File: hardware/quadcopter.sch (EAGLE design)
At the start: 56 parts, among them J1 AVR_SPI_PRG_6NS, J2 HEADER-4POS-2X2-0.1IN-FEMALE-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, J3 HEADER-10POSTH-254X10, J4 HEADER-4POS-0.1IN-FEMALE-SMD-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, Q1 MOSFET-SI2302CDS-T1-E3CT-ND, Q5 MOSFET-SI2302CDS-T1-E3CT-ND, Q6 MOSFET-SI2302CDS-T1-E3CT-ND, SW1 PUSHBUTTON_SMD-VERTICAL-1, U1 ATMEGA128RFA1, U2 LSM-IMU-497-18367-1-NDIMU, Y1 CRYSTAL5X3

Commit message: replaced motors
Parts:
- added MOTOR2, MOTOR3, MOTOR4: MOTOR_PADS_GND-MOLEX-SMD, quadparts_prebuilt_2022:MOTOR_PADS_GND-MOLEX-SMD
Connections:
- net BAT_GND: now also MOTOR2.GND, MOTOR3.GND, MOTOR4.GND
- net N$15: now also MOTOR2.V-
- net N$16: now also MOTOR3.V-
- net N$17: now also MOTOR4.V-
- net VBAT: now also MOTOR2.V+, MOTOR3.V+, MOTOR4.V+
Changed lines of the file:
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@@
 <part name="GND47" library="quadparts_prebuilt_2022" deviceset="GND" device=""/>
 <part name="P+22" library="quadparts_prebuilt_2022" deviceset="3V" device=""/>
+<part name="MOTOR2" library="quadparts_prebuilt_2022" deviceset="MOTOR_PADS_GND" device="-MOLEX-SMD"/>
+<part name="MOTOR3" library="quadparts_prebuilt_2022" deviceset="MOTOR_PADS_GND" device="-MOLEX-SMD"/>
+<part name="MOTOR4" library="quadparts_prebuilt_2022" deviceset="MOTOR_PADS_GND" device="-MOLEX-SMD"/>
 </parts>
 <sheets>
@@
 <attribute name="VALUE" x="256.54" y="27.94" size="1.778" layer="96" rot="R180" align="center"/>
 </instance>
+<instance part="MOTOR2" gate="G$1" x="55.88" y="27.94" smashed="yes">
+<attribute name="NAME" x="53.34" y="35.56" size="0.8128" layer="95"/>
+</instance>
+<instance part="MOTOR3" gate="G$1" x="104.14" y="27.94" smashed="yes">
+<attribute name="NAME" x="101.6" y="35.56" size="0.8128" layer="95"/>
+</instance>
+<instance part="MOTOR4" gate="G$1" x="154.94" y="27.94" smashed="yes">
+<attribute name="NAME" x="152.4" y="35.56" size="0.8128" layer="95"/>
+</instance>
 </instances>
 <busses>
@@
 <junction x="63.5" y="38.1"/>
 <pinref part="D4" gate="G$1" pin="C"/>
+<pinref part="MOTOR2" gate="G$1" pin="V+"/>
 </segment>
 <segment>
@@
 <junction x="111.76" y="38.1"/>
 <pinref part="D5" gate="G$1" pin="C"/>
+<pinref part="MOTOR3" gate="G$1" pin="V+"/>
 </segment>
 <segment>
@@
 <junction x="162.56" y="38.1"/>
 <pinref part="D6" gate="G$1" pin="C"/>
+<pinref part="MOTOR4" gate="G$1" pin="V+"/>
 </segment>
 <segment>
@@
 <pinref part="C15" gate="G$1" pin="2"/>
 </segment>
+<segment>
+<pinref part="GND23" gate="1" pin="BAT_GND"/>
+<pinref part="MOTOR2" gate="G$1" pin="GND"/>
+</segment>
+<segment>
+<pinref part="GND26" gate="1" pin="BAT_GND"/>
+<pinref part="MOTOR3" gate="G$1" pin="GND"/>
+</segment>
+<segment>
+<pinref part="GND29" gate="1" pin="BAT_GND"/>
+<pinref part="MOTOR4" gate="G$1" pin="GND"/>
+</segment>
 </net>
 <net name="PWM2" class="0">
@@
 <wire x1="86.36" y1="27.94" x2="86.36" y2="25.4" width="0.1524" layer="91"/>
 <pinref part="D4" gate="G$1" pin="A"/>
+<pinref part="MOTOR2" gate="G$1" pin="V-"/>
 </segment>
 </net>
@@
 <pinref part="D5" gate="G$1" pin="A"/>
 <junction x="124.46" y="27.94"/>
+<pinref part="MOTOR3" gate="G$1" pin="V-"/>
 </segment>
 </net>
@@
 <wire x1="185.42" y1="27.94" x2="185.42" y2="25.4" width="0.1524" layer="91"/>
 <pinref part="D6" gate="G$1" pin="A"/>
-</segment>
-</net>
+<pinref part="MOTOR4" gate="G$1" pin="V-"/>
+</segment>
+</net>

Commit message: replaced motor pads and mosfets fulls
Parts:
- added Q2, Q3, Q4: MOSFET-SI2302CDS-T1-E3CT-ND, custom_.lbr:MOSFET-SI2302CDS-T1-E3CT-ND
- renumbered FRONT-LEFT-MOTOR to U$1
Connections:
- net BAT_GND: now also Q2.S, Q3.S, Q4.S
- net N$15: now also Q2.D
- net N$16: now also Q3.D
- net N$17: now also Q4.D
- net PWM2: now also Q2.G
- net PWM3: now also Q3.G
- net PWM4: now also Q4.G
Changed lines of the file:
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@@
 <part name="GND18" library="quadparts_prebuilt_2022" deviceset="GND" device=""/>
 <part name="P+7" library="quadparts_prebuilt_2022" deviceset="3V" device=""/>
-<part name="FRONT-LEFT-MOTOR" library="quadparts_prebuilt_2022" deviceset="MOTOR_PADS_GND" device="-MOLEX-SMD"/>
 <part name="P+8" library="quadparts_prebuilt_2022" deviceset="VBAT" device=""/>
 <part name="D3" library="quadparts_prebuilt_2022" deviceset="DIODE-SCHOTTKY_" device="-SMD-SOD123" package3d_urn="urn:adsk.eagle:package:11793366/1" value="360mV"/>
@@
 <part name="GND21" library="quadparts_prebuilt_2022" deviceset="BAT_GND" device=""/>
 <part name="GND22" library="quadparts_prebuilt_2022" deviceset="GND" device=""/>
-<part name="Q1" library="custom_.lbr" library_urn="urn:adsk.wipprod:fs.file:vf.FjMADskDQ2Se9fX1PD5xcw" deviceset="MOSFET" device="-SI2302CDS-T1-E3CT-ND"/>
 <part name="P+9" library="quadparts_prebuilt_2022" deviceset="VBAT" device=""/>
 <part name="D4" library="quadparts_prebuilt_2022" deviceset="DIODE-SCHOTTKY_" device="-SMD-SOD123" package3d_urn="urn:adsk.eagle:package:11793366/1" value="360mV"/>
@@
 <part name="MOTOR3" library="quadparts_prebuilt_2022" deviceset="MOTOR_PADS_GND" device="-MOLEX-SMD"/>
 <part name="MOTOR4" library="quadparts_prebuilt_2022" deviceset="MOTOR_PADS_GND" device="-MOLEX-SMD"/>
+<part name="U$1" library="quadparts_prebuilt_2022" deviceset="MOTOR_PADS_GND" device="-MOLEX-SMD"/>
+<part name="Q1" library="custom_.lbr" library_urn="urn:adsk.wipprod:fs.file:vf.FjMADskDQ2Se9fX1PD5xcw" deviceset="MOSFET" device="-SI2302CDS-T1-E3CT-ND"/>
+<part name="Q2" library="custom_.lbr" library_urn="urn:adsk.wipprod:fs.file:vf.FjMADskDQ2Se9fX1PD5xcw" deviceset="MOSFET" device="-SI2302CDS-T1-E3CT-ND"/>
+<part name="Q3" library="custom_.lbr" library_urn="urn:adsk.wipprod:fs.file:vf.FjMADskDQ2Se9fX1PD5xcw" deviceset="MOSFET" device="-SI2302CDS-T1-E3CT-ND"/>
+<part name="Q4" library="custom_.lbr" library_urn="urn:adsk.wipprod:fs.file:vf.FjMADskDQ2Se9fX1PD5xcw" deviceset="MOSFET" device="-SI2302CDS-T1-E3CT-ND"/>
 </parts>
 <sheets>
@@
 <attribute name="VALUE" x="287.02" y="162.56" size="1.778" layer="96" rot="R180" align="center"/>
 </instance>
-<instance part="FRONT-LEFT-MOTOR" gate="G$1" x="7.62" y="27.94" smashed="yes">
-<attribute name="NAME" x="5.08" y="35.56" size="0.8128" layer="95"/>
-</instance>
 <instance part="P+8" gate="VCC" x="-2.54" y="43.18" smashed="yes">
 <attribute name="VALUE" x="-2.54" y="45.72" size="1.778" layer="96" rot="R180" align="center"/>
@@
 <attribute name="VALUE" x="10.16" y="-5.08" size="1.778" layer="96" align="center"/>
 </instance>
-<instance part="Q1" gate="G$1" x="35.56" y="15.24" smashed="yes">
-<attribute name="NAME" x="27.94" y="20.32" size="1.778" layer="95"/>
-</instance>
 <instance part="P+9" gate="VCC" x="45.72" y="43.18" smashed="yes">
 <attribute name="VALUE" x="45.72" y="45.72" size="1.778" layer="96" rot="R180" align="center"/>
@@
 <instance part="MOTOR4" gate="G$1" x="154.94" y="27.94" smashed="yes">
 <attribute name="NAME" x="152.4" y="35.56" size="0.8128" layer="95"/>
+</instance>
+<instance part="U$1" gate="G$1" x="7.62" y="27.94" smashed="yes">
+<attribute name="NAME" x="5.08" y="35.56" size="0.8128" layer="95"/>
+</instance>
+<instance part="Q1" gate="G$1" x="35.56" y="15.24" smashed="yes">
+<attribute name="NAME" x="27.94" y="20.32" size="1.778" layer="95"/>
+</instance>
+<instance part="Q2" gate="G$1" x="83.82" y="15.24" smashed="yes">
+<attribute name="NAME" x="76.2" y="20.32" size="1.778" layer="95"/>
+</instance>
+<instance part="Q3" gate="G$1" x="132.08" y="15.24" smashed="yes">
+<attribute name="NAME" x="124.46" y="20.32" size="1.778" layer="95"/>
+</instance>
+<instance part="Q4" gate="G$1" x="182.88" y="15.24" smashed="yes">
+<attribute name="NAME" x="175.26" y="20.32" size="1.778" layer="95"/>
 </instance>
 </instances>
@@
 <net name="VBAT" class="0">
 <segment>
-<pinref part="FRONT-LEFT-MOTOR" gate="G$1" pin="V+"/>
 <wire x1="15.24" y1="33.02" x2="15.24" y2="38.1" width="0.1524" layer="91" style="longdash"/>
 <wire x1="15.24" y1="38.1" x2="-2.54" y2="38.1" width="0.1524" layer="91"/>
@@
 <pinref part="D3" gate="G$1" pin="C"/>
 <pinref part="C12" gate="G$1" pin="+"/>
+<pinref part="U$1" gate="G$1" pin="V+"/>
 </segment>
 <segment>
@@
 <wire x1="27.94" y1="30.48" x2="27.94" y2="27.94" width="0.1524" layer="91"/>
 <wire x1="27.94" y1="27.94" x2="15.24" y2="27.94" width="0.1524" layer="91"/>
-<pinref part="FRONT-LEFT-MOTOR" gate="G$1" pin="V-"/>
 <wire x1="27.94" y1="27.94" x2="38.1" y2="27.94" width="0.1524" layer="91"/>
 <junction x="27.94" y="27.94"/>
 <wire x1="38.1" y1="27.94" x2="38.1" y2="25.4" width="0.1524" layer="91"/>
+<pinref part="D3" gate="G$1" pin="A"/>
+<pinref part="U$1" gate="G$1" pin="V-"/>
 <pinref part="Q1" gate="G$1" pin="D"/>
-<pinref part="D3" gate="G$1" pin="A"/>
 </segment>
 </net>
 <net name="BAT_GND" class="0">
 <segment>
-<pinref part="FRONT-LEFT-MOTOR" gate="G$1" pin="GND"/>
 <pinref part="GND20" gate="1" pin="BAT_GND"/>
 <wire x1="-5.08" y1="25.4" x2="-5.08" y2="22.86" width="0.1524" layer="91"/>
 <wire x1="-5.08" y1="22.86" x2="7.62" y2="22.86" width="0.1524" layer="91"/>
+<pinref part="C12" gate="G$1" pin="-"/>
+<pinref part="U$1" gate="G$1" pin="GND"/>
 <junction x="7.62" y="22.86"/>
-<pinref part="C12" gate="G$1" pin="-"/>
-</segment>
-<segment>
-<pinref part="Q1" gate="G$1" pin="S"/>
+</segment>
+<segment>
 <wire x1="38.1" y1="5.08" x2="27.94" y2="5.08" width="0.1524" layer="91"/>
 <pinref part="GND21" gate="1" pin="BAT_GND"/>
+<pinref part="Q1" gate="G$1" pin="S"/>
 </segment>
 <segment>
 <wire x1="86.36" y1="5.08" x2="76.2" y2="5.08" width="0.1524" layer="91"/>
 <pinref part="GND24" gate="1" pin="BAT_GND"/>
+<pinref part="Q2" gate="G$1" pin="S"/>
 </segment>
 <segment>
 <wire x1="134.62" y1="5.08" x2="124.46" y2="5.08" width="0.1524" layer="91"/>
 <pinref part="GND27" gate="1" pin="BAT_GND"/>
+<pinref part="Q3" gate="G$1" pin="S"/>
 </segment>
 <segment>
 <wire x1="185.42" y1="5.08" x2="175.26" y2="5.08" width="0.1524" layer="91"/>
 <pinref part="GND30" gate="1" pin="BAT_GND"/>
+<pinref part="Q4" gate="G$1" pin="S"/>
 </segment>
 <segment>
@@
 <label x="66.04" y="22.86" size="1.016" layer="95" rot="R180" xref="yes"/>
 <pinref part="R7" gate="G$1" pin="1"/>
+<pinref part="Q2" gate="G$1" pin="G"/>
 </segment>
 <segment>
@@
 <pinref part="D4" gate="G$1" pin="A"/>
 <pinref part="MOTOR2" gate="G$1" pin="V-"/>
+<pinref part="Q2" gate="G$1" pin="D"/>
 </segment>
 </net>
@@
 <junction x="124.46" y="27.94"/>
 <pinref part="MOTOR3" gate="G$1" pin="V-"/>
+<pinref part="Q3" gate="G$1" pin="D"/>
 </segment>
 </net>
@@
 <pinref part="D6" gate="G$1" pin="A"/>
 <pinref part="MOTOR4" gate="G$1" pin="V-"/>
+<pinref part="Q4" gate="G$1" pin="D"/>
 </segment>
 </net>
 <net name="PWM1" class="0">
 <segment>
-<pinref part="Q1" gate="G$1" pin="G"/>
 <wire x1="25.4" y1="15.24" x2="22.86" y2="15.24" width="0.1524" layer="91"/>
 <wire x1="22.86" y1="15.24" x2="22.86" y2="22.86" width="0.1524" layer="91"/>
@@
 <label x="17.78" y="22.86" size="1.016" layer="95" rot="R180" xref="yes"/>
 <pinref part="R6" gate="G$1" pin="1"/>
+<pinref part="Q1" gate="G$1" pin="G"/>
 </segment>
 <segment>
@@
 <label x="114.3" y="22.86" size="1.016" layer="95" rot="R180" xref="yes"/>
 <pinref part="R8" gate="G$1" pin="1"/>
+<pinref part="Q3" gate="G$1" pin="G"/>
 </segment>
 <segment>
@@
 <label x="165.1" y="22.86" size="1.016" layer="95" rot="R180" xref="yes"/>
 <pinref part="R9" gate="G$1" pin="1"/>
-</segment>
-<segment>
+<pinref part="Q4" gate="G$1" pin="G"/>
+</segment>
+<segment>

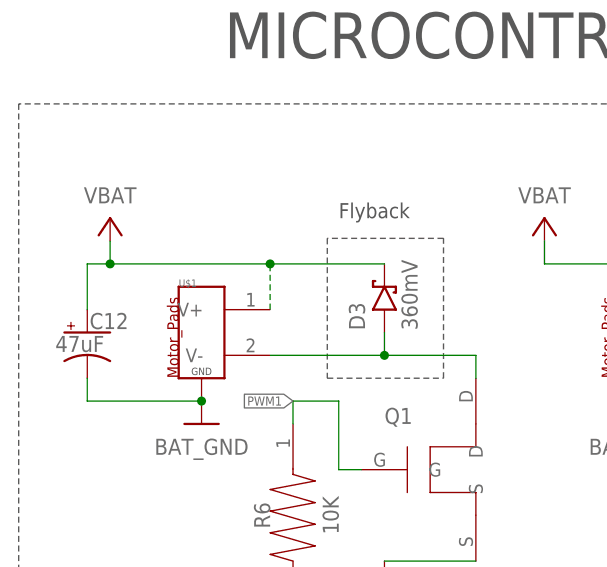
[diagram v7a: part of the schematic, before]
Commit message: replaced flyback diodes
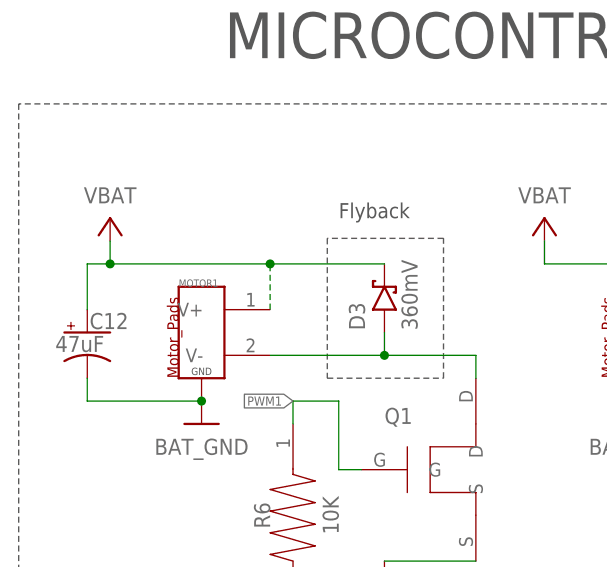
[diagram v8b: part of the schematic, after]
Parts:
- D3, D4, D5, D6: device quadparts_prebuilt_2022:DIODE-SCHOTTKY_-SMD-SOD123 -> quadparts_prebuilt_2022:DIODE-SCHOTTKY_SMD-SOD123-360MV-OLD
- renumbered U$1 to MOTOR1
